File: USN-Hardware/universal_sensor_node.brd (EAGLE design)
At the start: 20.3 x 31.9 mm, 20 parts, among them J2 SSQ-110-03-T-S, J3 JST_S2B-ZR-SM4A-TF_LF_SNJST_S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, J4 10118192-0001LF, J5 SSQ-110-03-T-S, U1 MCP73831T-2ACI/OT, U2 ATMEGA328PB-AU, Y1 TSX-3225EPSON_TSX-3225_16.000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

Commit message: looks good to me.  Placed order with oshpark
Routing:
- net N$26: track 0.00 -> 11.7 mm, vias 0 -> 1
- net N$27: track 0.00 -> 4.95 mm, vias 0 -> 1
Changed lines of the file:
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@@
 <text x="3.175" y="24.638" size="0.762" layer="25" font="vector" ratio="10">GND</text>
 <text x="3.175" y="4.445" size="0.762" layer="25" font="vector" ratio="10">DTR</text>
-<text x="3.302" y="1.524" size="0.762" layer="27" font="vector" ratio="10">3V7</text>
-<text x="3.048" y="9.398" size="0.762" layer="27" font="vector" ratio="10">TX</text>
-<text x="3.302" y="6.985" size="0.762" layer="27" font="vector" ratio="10">RX</text>
+<text x="3.302" y="1.524" size="0.762" layer="21" font="vector" ratio="10">3V7</text>
+<text x="3.048" y="9.398" size="0.762" layer="21" font="vector" ratio="10">TX</text>
+<text x="3.302" y="6.985" size="0.762" layer="21" font="vector" ratio="10">RX</text>
 <text x="3.175" y="22.098" size="0.762" layer="21" font="vector" ratio="10">SS</text>
 <text x="3.175" y="19.685" size="0.762" layer="21" font="vector" ratio="10">MOSI</text>
@@
 <text x="6.477" y="5.969" size="0.889" layer="25">CHRG</text>
 <text x="11.176" y="5.969" size="0.889" layer="25">FULL</text>
-<text x="15.621" y="24.765" size="0.762" layer="25">GND</text>
-<text x="16.51" y="22.098" size="0.762" layer="25">D3</text>
-<text x="15.875" y="1.778" size="0.762" layer="27" font="vector" ratio="10">3V7</text>
+<text x="15.875" y="1.778" size="0.762" layer="21" font="vector" ratio="10">3V7</text>
 <text x="15.367" y="9.271" size="0.762" layer="21" font="vector" ratio="10">ADC2</text>
+<text x="15.875" y="24.765" size="0.762" layer="25" font="vector" ratio="10">GND</text>
+<text x="16.637" y="21.971" size="0.762" layer="25" font="vector" ratio="10">D3</text>
 </plain>
 <attributes>
@@
 </class>
 </classes>
-<designrules name="oshpark-2layer *">
-<description language="de">&lt;b&gt;EAGLE Design Rules&lt;/b&gt;
+<designrules name="oshpark-2layer">
+<description language="en">&lt;b&gt;OSH Park Design Rules&lt;/b&gt;
 &lt;p&gt;
-Die Standard-Design-Rules sind so gewählt, dass sie für
-die meisten Anwendungen passen. Sollte ihre Platine
-besondere Anforderungen haben, treffen Sie die erforderlichen
-Einstellungen hier und speichern die Design Rules unter
-einem neuen Namen ab.</description>
-<description language="en">&lt;b&gt;Laen's PCB Order Design Rules&lt;/b&gt;
+Please make sure your boards conform to these design rules.
+&lt;/p&gt;
 &lt;p&gt;
-Please make sure your boards conform to these design rules.</description>
+Note, that not all DRC settings must be set by the manufacturer. Several can be adjusted for the design, including those listed on our docs page here.
+&lt;a href=&quot;http://docs.oshpark.com/design-tools/eagle/design-rules-files/&quot;&gt;Adjustable Settings&lt;/a&gt;
+&lt;/p&gt;</description>
 <param name="layerSetup" value="(1*16)"/>
-<param name="mtCopper" value="0.0356mm 0.0356mm 0.0356mm 0.0356mm 0.0356mm 0.0356mm 0.0356mm 0.0356mm 0.0356mm 0.0356mm 0.0356mm 0.0356mm 0.0356mm 0.0356mm 0.0356mm 0.0356mm"/>
-<param name="mtIsolate" value="1.5011mm 0.1499mm 0.2007mm 0.1499mm 0.2007mm 0.1499mm 0.2007mm 0.1499mm 0.2007mm 0.1499mm 0.2007mm 0.1499mm 0.2007mm 0.1499mm 0.2007mm"/>
-<param name="mdWireWire" value="8mil"/>
-<param name="mdWirePad" value="7mil"/>
-<param name="mdWireVia" value="7mil"/>
+<param name="mtCopper" value="0.035559375mm 0.0356mm 0.0356mm 0.0356mm 0.0356mm 0.0356mm 0.0356mm 0.0356mm 0.0356mm 0.0356mm 0.0356mm 0.0356mm 0.0356mm 0.0356mm 0.0356mm 0.035559375mm"/>
+<param name="mtIsolate" value="1.6mm 0.1499mm 0.2007mm 0.1499mm 0.2007mm 0.1499mm 0.2007mm 0.1499mm 0.2007mm 0.1499mm 0.2007mm 0.1499mm 0.2007mm 0.1499mm 0.2007mm"/>
+<param name="mdWireWire" value="6mil"/>
+<param name="mdWirePad" value="6mil"/>
+<param name="mdWireVia" value="6mil"/>
 <param name="mdPadPad" value="6mil"/>
-<param name="mdPadVia" value="7mil"/>
-<param name="mdViaVia" value="7mil"/>
+<param name="mdPadVia" value="6mil"/>
+<param name="mdViaVia" value="6mil"/>
 <param name="mdSmdPad" value="6mil"/>
 <param name="mdSmdVia" value="6mil"/>
@@
 <param name="mdSmdStop" value="0mil"/>
 <param name="msWidth" value="6mil"/>
-<param name="msDrill" value="15mil"/>
-<param name="msMicroVia" value="15mil"/>
+<param name="msDrill" value="10mil"/>
+<param name="msMicroVia" value="10mil"/>
 <param name="msBlindViaRatio" value="0.5"/>
 <param name="rvPadTop" value="0.25"/>
@@
 <param name="rvMicroViaOuter" value="0.25"/>
 <param name="rvMicroViaInner" value="0.25"/>
-<param name="rlMinPadTop" value="7mil"/>
+<param name="rlMinPadTop" value="5mil"/>
 <param name="rlMaxPadTop" value="20mil"/>
-<param name="rlMinPadInner" value="7mil"/>
+<param name="rlMinPadInner" value="5mil"/>
 <param name="rlMaxPadInner" value="20mil"/>
-<param name="rlMinPadBottom" value="7mil"/>
+<param name="rlMinPadBottom" value="5mil"/>
 <param name="rlMaxPadBottom" value="20mil"/>
-<param name="rlMinViaOuter" value="7mil"/>
+<param name="rlMinViaOuter" value="5mil"/>
 <param name="rlMaxViaOuter" value="20mil"/>
-<param name="rlMinViaInner" value="7mil"/>
+<param name="rlMinViaInner" value="5mil"/>
 <param name="rlMaxViaInner" value="20mil"/>
-<param name="rlMinMicroViaOuter" value="4mil"/>
+<param name="rlMinMicroViaOuter" value="5mil"/>
 <param name="rlMaxMicroViaOuter" value="20mil"/>
-<param name="rlMinMicroViaInner" value="4mil"/>
+<param name="rlMinMicroViaInner" value="5mil"/>
 <param name="rlMaxMicroViaInner" value="20mil"/>
 <param name="psTop" value="-1"/>
@@
 <param name="mlMinCreamFrame" value="0mil"/>
 <param name="mlMaxCreamFrame" value="0mil"/>
-<param name="mlViaStopLimit" value="16mil"/>
+<param name="mlViaStopLimit" value="0mil"/>
 <param name="srRoundness" value="0"/>
 <param name="srMinRoundness" value="0mil"/>
@@
 <via x="4.826" y="0.762" extent="1-16" drill="0.381"/>
 <wire x1="4.826" y1="0.762" x2="6.477" y2="0.762" width="0.381" layer="16"/>
-<wire x1="6.77" y1="1.055" x2="6.77" y2="3.81" width="0.381" layer="16"/>
 <wire x1="6.477" y1="0.762" x2="6.77" y2="1.055" width="0.381" layer="16"/>
 <wire x1="6.77" y1="3.81" x2="6.77" y2="5.168" width="0.381" layer="16"/>
@@
 <wire x1="6.731" y1="5.207" x2="7.405" y2="5.881" width="0.1524" layer="1"/>
 <wire x1="7.405" y1="5.881" x2="7.405" y2="7.493" width="0.1524" layer="1"/>
-<wire x1="6.77" y1="3.81" x2="6.77" y2="1.778" width="0" layer="19" extent="16-16"/>
+<wire x1="6.77" y1="1.055" x2="6.77" y2="1.778" width="0.381" layer="16"/>
+<wire x1="6.77" y1="1.778" x2="6.77" y2="3.81" width="0.381" layer="16"/>
 </signal>
 <signal name="GND">
@@
 <contactref element="C4" pad="2"/>
 <contactref element="Y1" pad="2"/>
-<contactref element="R5" pad="1"/>
-<contactref element="C7" pad="2"/>
-<contactref element="C9" pad="2"/>
 <contactref element="C6" pad="2"/>
 <contactref element="C8" pad="2"/>
@@
 <vertex x="0.381" y="-5.08"/>
 </polygon>
-<wire x1="8.47" y1="1.778" x2="8.851" y2="0.762" width="0" layer="19" extent="1-16"/>
+<via x="6.35" y="20.574" extent="1-16" drill="0.381"/>
+<via x="11.811" y="-0.889" extent="1-16" drill="0.381"/>
+<via x="13.208" y="3.302" extent="1-16" drill="0.381"/>
+<contactref element="C7" pad="2"/>
+<contactref element="C9" pad="2"/>
+<contactref element="R5" pad="1"/>
 </signal>
 <signal name="NC13">
@@
 <contactref element="Y1" pad="1"/>
 <contactref element="C4" pad="1"/>
-<wire x1="7.912" y1="17.102" x2="7.962" y2="19.304" width="0" layer="19" extent="16-16"/>
-<wire x1="6.044078125" y1="16.527490625" x2="7.912" y2="17.102" width="0" layer="19" extent="1-16"/>
+<wire x1="7.962" y1="19.304" x2="7.962" y2="17.102" width="0.1524" layer="16"/>
+<wire x1="7.962" y1="17.102" x2="7.912" y2="17.102" width="0.1524" layer="16"/>
+<wire x1="6.044078125" y1="16.527490625" x2="6.044078125" y2="16.94666875" width="0.1524" layer="1"/>
+<wire x1="6.044078125" y1="16.94666875" x2="4.859025" y2="18.131721875" width="0.1524" layer="1"/>
+<wire x1="4.859025" y1="20.277946875" x2="5.917078125" y2="21.336" width="0.1524" layer="1"/>
+<via x="7.747" y="20.701" extent="1-16" drill="0.381"/>
+<wire x1="7.747" y1="20.701" x2="7.962" y2="20.701" width="0.1524" layer="16"/>
+<wire x1="7.962" y1="20.701" x2="7.962" y2="19.304" width="0.1524" layer="16"/>
+<wire x1="4.859025" y1="18.131721875" x2="4.859025" y2="20.277946875" width="0.1524" layer="1"/>
+<wire x1="7.112" y1="21.336" x2="5.917078125" y2="21.336" width="0.1524" layer="1"/>
+<wire x1="7.112" y1="21.336" x2="7.747" y2="20.701" width="0.1524" layer="1"/>
 </signal>
 <signal name="N$27">
@@
 <contactref element="Y1" pad="3"/>
 <contactref element="C5" pad="1"/>
-<wire x1="6.312" y1="14.899" x2="5.47839375" y2="15.96180625" width="0" layer="19" extent="1-16"/>
-<wire x1="6.262" y1="12.827" x2="6.312" y2="14.899" width="0" layer="19" extent="16-16"/>
+<wire x1="5.47839375" y1="15.96180625" x2="5.01035625" y2="15.96180625" width="0.1524" layer="1"/>
+<wire x1="5.01035625" y1="15.96180625" x2="5.01035625" y2="14.986" width="0.1524" layer="1"/>
+<via x="5.01035625" y="14.986" extent="1-16" drill="0.381"/>
+<wire x1="5.01035625" y1="14.986" x2="6.312" y2="14.986" width="0.1524" layer="16"/>
+<wire x1="6.312" y1="14.986" x2="6.312" y2="14.899" width="0.1524" layer="16"/>
+<wire x1="6.312" y1="14.899" x2="6.312" y2="12.827" width="0.1524" layer="16"/>
+<wire x1="6.312" y1="12.827" x2="6.262" y2="12.827" width="0.1524" layer="16"/>
 </signal>
 <signal name="N$11">

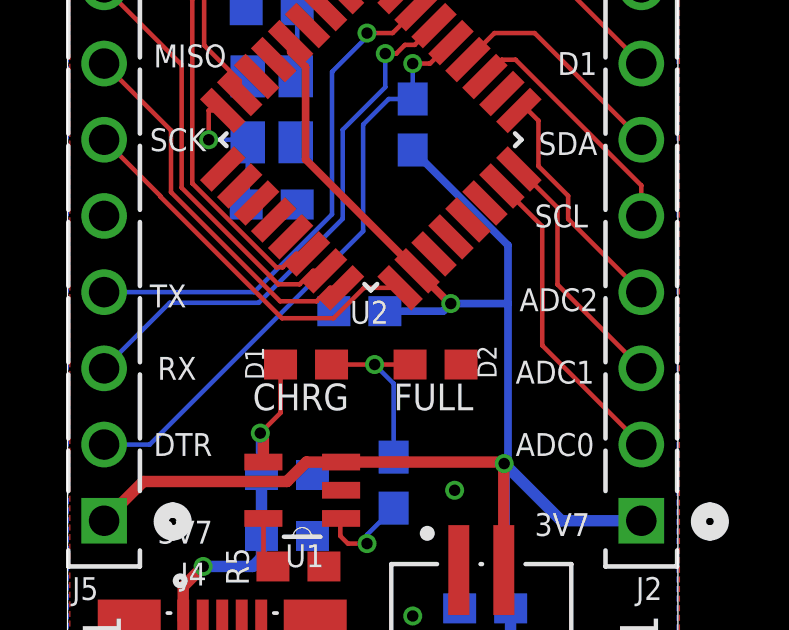
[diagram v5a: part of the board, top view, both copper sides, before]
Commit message: updated parts attributes for bom.
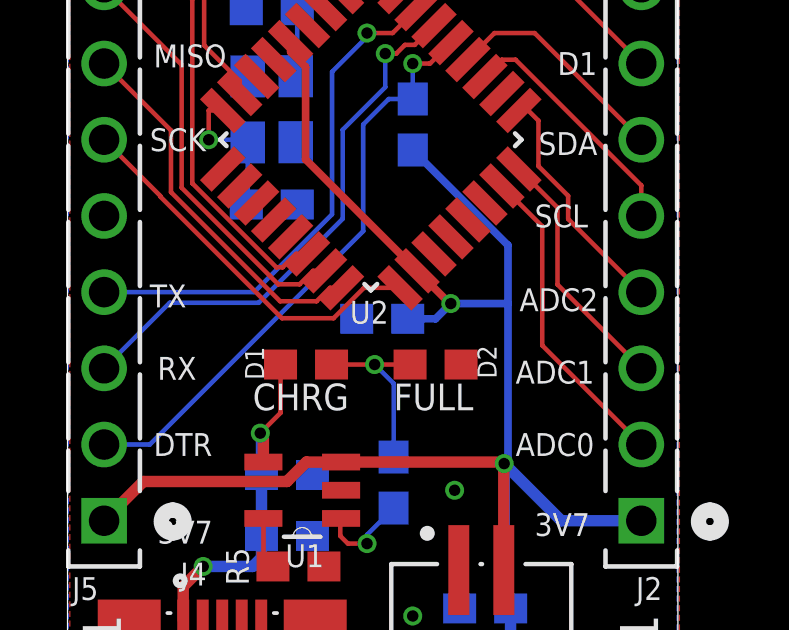
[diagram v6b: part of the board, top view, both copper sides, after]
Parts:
- removed C3: 100nF, universal_sensor_node:0603-CAP
- added C1: 100nF, universal_sensor_node:0603-CAP
- U2: device ATMEGA328PB-AU:QFP80P900X900X120-32N -> universal_sensor_node:QFP80P900X900X120-32N
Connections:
- net 3V7: now also C1.1; no longer C3.1
- net GND: now also C1.2; no longer C3.2
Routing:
- net 3V7: track 57.1 -> 56.4 mm
